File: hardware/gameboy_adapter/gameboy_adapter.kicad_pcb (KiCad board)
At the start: 2 copper layers, 97 x 34 mm, 3 parts, among them J1 CART SLOT TOP ROW, J2 GBA_Slot, SW1 SW_SPDT

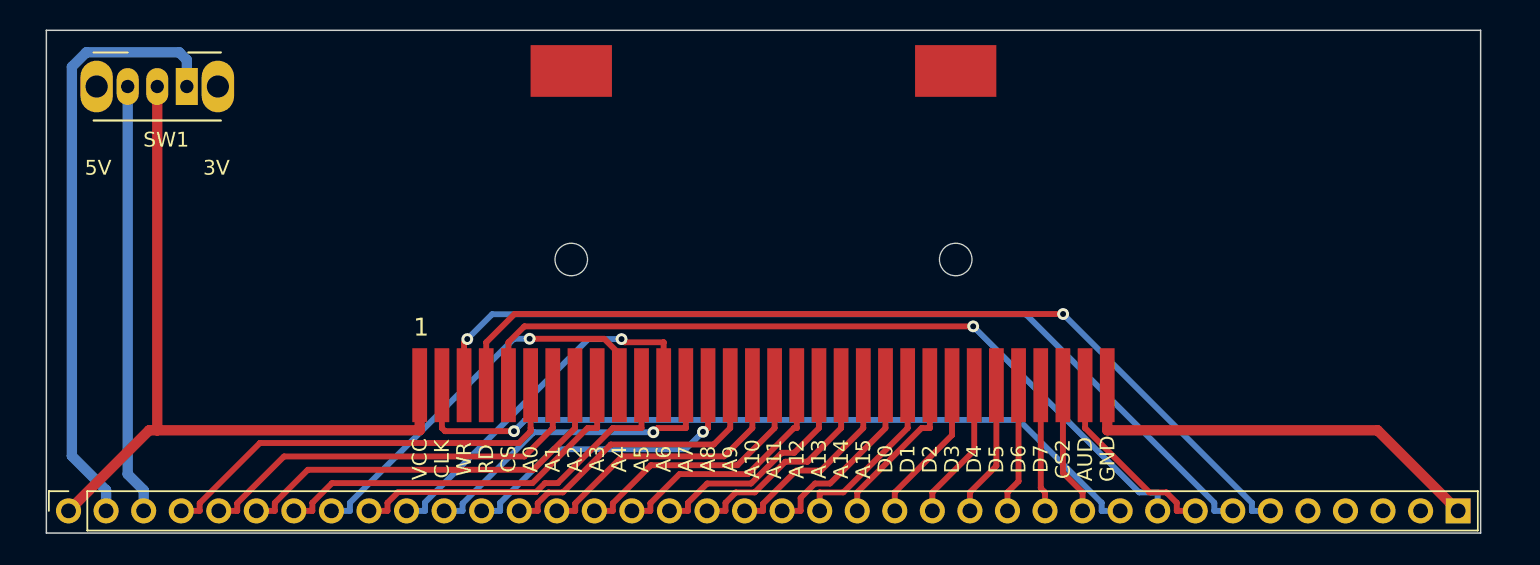
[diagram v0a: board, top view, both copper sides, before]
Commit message: Add mounting holes to Game Boy adapter
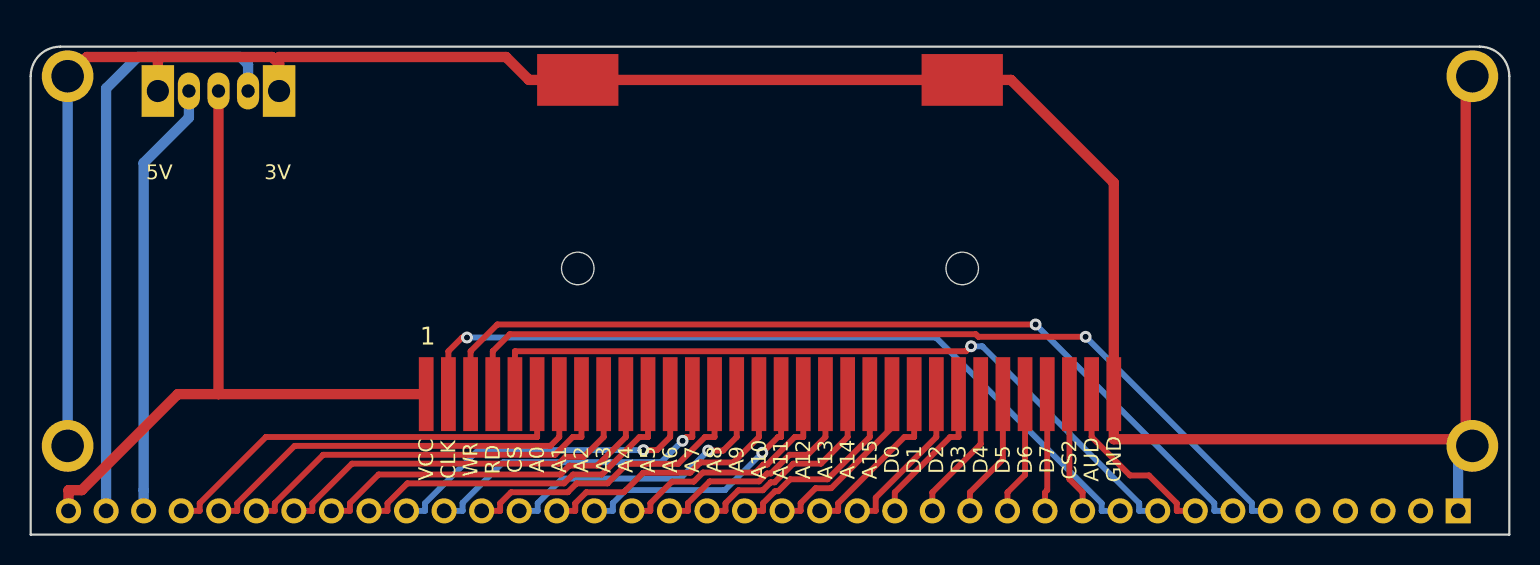
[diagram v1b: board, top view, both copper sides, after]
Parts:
- added M2_1: Screw_Terminal_01x01, MountingHole:MountingHole_2.2mm_M2_ISO7380_Pad, F.Cu at (102.5, 52.0)
- added M2_10: Screw_Terminal_01x01, MountingHole:MountingHole_2.2mm_M2_ISO7380_Pad, F.Cu at (102.5, 77.0)
- added M2_2: Screw_Terminal_01x01, MountingHole:MountingHole_2.2mm_M2_ISO7380_Pad, F.Cu at (197.5, 52.0)
- added M2_3: Screw_Terminal_01x01, MountingHole:MountingHole_2.2mm_M2_ISO7380_Pad, F.Cu at (197.5, 77.0)
- moved SW1 4.15 mm to (114.7, 53.0)
- moved J2 0.75 mm to (150.0, 68.5)
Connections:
- J2 pad SHIELD_3: (no net) -> GND
- J2 pad SHIELD_4: (no net) -> GND
- SW1 pad : (no net) -> GND
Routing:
- net GND: track 29.0 -> 175.9 mm
- net VCC: track 52.3 -> 48.8 mm
- net A6: track 25.5 -> 23.1 mm
- net A4: track 27.2 -> 25.2 mm, vias 1 -> 0
- net D16: track 52.0 -> 53.9 mm
- net D6: track 53.2 -> 51.4 mm
- net D9: track 62.6 -> 61.2 mm
- net D17: track 9.05 -> 8.26 mm
- net D8: track 61.5 -> 60.7 mm
- net D7: track 13.0 -> 12.3 mm
- net D30: track 8.62 -> 7.96 mm
- net +5V: track 29.1 -> 29.7 mm
- net A11: track 17.7 -> 17.9 mm, vias 0 -> 1
- net A9: track 19.8 -> 20.0 mm, vias 0 -> 1
- net A8: track 20.9 -> 21.0 mm, vias 1 -> 0
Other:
- board size 97 x 34 mm -> 100 x 33 mm
- board text added: "G"
- board text added: "V"
